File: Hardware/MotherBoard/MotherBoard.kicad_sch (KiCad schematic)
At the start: 16 parts, among them J1 POWER, J10 I/O_PWR, J2 I/O0, J5 I/O1, J6 EXTRN_CLCK, U1 AMS1117-5.0

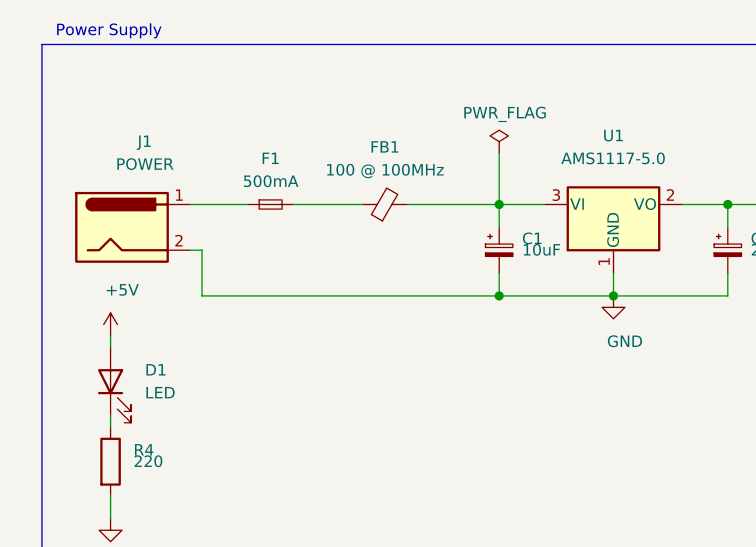
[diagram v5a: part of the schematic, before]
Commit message: Implement DMA and PCB ports
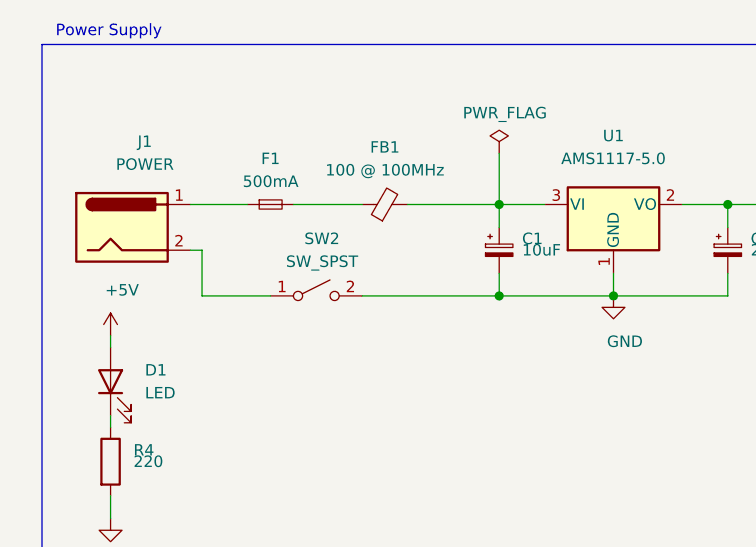
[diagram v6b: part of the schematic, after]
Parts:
- added SW2: SW_SPST, Button_Switch_THT:SW_E-Switch_EG1224_SPDT_Angled, symbol Switch:SW_SPST
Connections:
- net GND: now also SW2.2 (B); no longer J1.2
- new net: J1.2, SW2.1 (A)
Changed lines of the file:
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@@
     (company "Romuald Rousseau")
   )
+  (bus_alias "A12" (members "A12"))
   (bus_alias "A11" (members "A11"))
-  (bus_alias "A12" (members "A12"))
   (junction (at 76.835 47.625) (diameter 1.016) (color 0 0 0 0))
   (junction (at 76.835 57.785) (diameter 1.016) (color 0 0 0 0))
@@
     (stroke (width 0) (type solid) (color 0 0 0 0))
   )
-  (wire (pts (xy 43.815 57.785) (xy 76.835 57.785))
+  (wire (pts (xy 43.815 57.785) (xy 51.435 57.785))
     (stroke (width 0) (type solid) (color 0 0 0 0))
   )
   (wire (pts (xy 53.975 47.625) (xy 61.595 47.625))
+    (stroke (width 0) (type solid) (color 0 0 0 0))
+  )
+  (wire (pts (xy 61.595 57.785) (xy 76.835 57.785))
     (stroke (width 0) (type solid) (color 0 0 0 0))
   )
@@
     )
     (property "Datasheet" "~" (id 3) (at 33.655 67.31 0)
+      (effects (font (size 1.27 1.27)) hide)
+    )
+  )
+  (symbol (lib_id "Switch:SW_SPST") (at 56.515 57.785 0) (unit 1)
+    (in_bom yes) (on_board yes)
+    (property "Reference" "SW2" (id 0) (at 57.15 51.435 0))
+    (property "Value" "SW_SPST" (id 1) (at 57.15 53.975 0))
+    (property "Footprint" "Button_Switch_THT:SW_E-Switch_EG1224_SPDT_Angled" (id 2) (at 56.515 57.785 0)
+      (effects (font (size 1.27 1.27)) hide)
+    )
+    (property "Datasheet" "~" (id 3) (at 56.515 57.785 0)
       (effects (font (size 1.27 1.27)) hide)
     )
@@
       (reference "R4") (unit 1) (value "220") (footprint "Resistor_THT:R_Axial_DIN0207_L6.3mm_D2.5mm_P10.16mm_Horizontal")
     )
+    (path "/ff7dba36-e011-4018-9878-20ec48c66f8c"
+      (reference "SW2") (unit 1) (value "SW_SPST") (footprint "Button_Switch_THT:SW_E-Switch_EG1224_SPDT_Angled")
+    )
     (path "/4bb875c6-ec17-489d-8848-a58782a512d1"
       (reference "U1") (unit 1) (value "AMS1117-5.0") (footprint "Package_TO_SOT_THT:TO-220-3_Horizontal_TabDown")
@@
       (reference "#PWR0120") (unit 1) (value "GND") (footprint "")
     )
+    (path "/61215041-7d34-4941-9afc-8a556d19a10e/fa8f244d-8541-48fd-8737-6f2ca9b67fa3"
+      (reference "#PWR0133") (unit 1) (value "+5V") (footprint "")
+    )
+    (path "/61215041-7d34-4941-9afc-8a556d19a10e/a07bb74b-eddd-4abc-a5b3-41726b4489b6"
+      (reference "#PWR0134") (unit 1) (value "+5V") (footprint "")
+    )
     (path "/61215041-7d34-4941-9afc-8a556d19a10e/f636ab65-9304-4605-a863-9df3dd0ac4b4"
       (reference "C3") (unit 1) (value "10uF") (footprint "Capacitor_THT:C_Radial_D5.0mm_H11.0mm_P2.00mm")
@@
       (reference "J9") (unit 1) (value "Conn_02x02_Odd_Even") (footprint "Connector_PinHeader_2.54mm:PinHeader_2x02_P2.54mm_Vertical")
     )
+    (path "/61215041-7d34-4941-9afc-8a556d19a10e/0b60bde2-4a50-4611-bec5-b23ac5b9a520"
+      (reference "J11") (unit 1) (value "RDY_PULLUP") (footprint "")
+    )
+    (path "/61215041-7d34-4941-9afc-8a556d19a10e/6014f801-bb1a-4e11-b189-6e0f7a468124"
+      (reference "J12") (unit 1) (value "NMI_PULLUP") (footprint "")
+    )
     (path "/61215041-7d34-4941-9afc-8a556d19a10e/296fe1d1-b4f3-406e-be74-c856810e239d"
       (reference "R1") (unit 1) (value "10K") (footprint "Resistor_THT:R_Axial_DIN0207_L6.3mm_D2.5mm_P10.16mm_Horizontal")
@@
       (reference "R3") (unit 1) (value "10K") (footprint "Resistor_THT:R_Axial_DIN0207_L6.3mm_D2.5mm_P10.16mm_Horizontal")
     )
+    (path "/61215041-7d34-4941-9afc-8a556d19a10e/faba855d-d503-4563-a655-ff79b24d55c8"
+      (reference "R5") (unit 1) (value "10K") (footprint "Resistor_THT:R_Axial_DIN0207_L6.3mm_D2.5mm_P10.16mm_Horizontal")
+    )
     (path "/61215041-7d34-4941-9afc-8a556d19a10e/25f68c31-273a-4a47-b1bc-310d19fac600"
-      (reference "SW1") (unit 1) (value "RESET_SW") (footprint "Button_Switch_THT:SW_PUSH_6mm_H5mm")
+      (reference "SW1") (unit 1) (value "RESET_SW") (footprint "Button_Switch_THT:SW_Tactile_SPST_Angled_PTS645Vx83-2LFS")
     )
     (path "/61215041-7d34-4941-9afc-8a556d19a10e/6cd92b81-0135-4e6c-929c-13ce504ee354"
@@
       (reference "J8") (unit 1) (value "ISA11") (footprint "Connector_PinSocket_2.54mm:PinSocket_1x16_P2.54mm_Vertical")
     )
-    (path "/6cbd16f3-a1f6-4857-8623-5a6775377a9a/1e640dc0-9a9b-4e78-97a7-c4c4fba75621"
-      (reference "U9") (unit 1) (value "74HCT541") (footprint "Package_DIP:DIP-20_W7.62mm")
-    )
-    (path "/6cbd16f3-a1f6-4857-8623-5a6775377a9a/87eea902-e28a-40ef-a5ce-0c008a75322f"
-      (reference "U10") (unit 1) (value "74HCT541") (footprint "Package_DIP:DIP-20_W7.62mm")
+    (path "/6cbd16f3-a1f6-4857-8623-5a6775377a9a/3e3baca0-beca-49b0-b567-bf7be578d698"
+      (reference "U9") (unit 1) (value "SN74LVC245AN") (footprint "Package_DIP:DIP-20_W7.62mm")
+    )
+    (path "/6cbd16f3-a1f6-4857-8623-5a6775377a9a/b9a3a795-f7ea-4f67-9322-90ba34134211"
+      (reference "U10") (unit 1) (value "SN74LVC245AN") (footprint "Package_DIP:DIP-20_W7.62mm")
     )
     (path "/6cbd16f3-a1f6-4857-8623-5a6775377a9a/e8617ace-d039-40cf-88f5-54844f714e69"

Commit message: Version 1.2
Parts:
- added J11: RDY_PULLUP, Connector_PinHeader_2.54mm:PinHeader_1x02_P2.54mm_Vertical, symbol Connector:Conn_01x02_Male
- added J12: NMI_PULLUP, Connector_PinHeader_2.54mm:PinHeader_1x02_P2.54mm_Vertical, symbol Connector:Conn_01x02_Male
- added J13: USB_OTG, Connector_USB:USB_B_OST_USB-B1HSxx_Horizontal, symbol Connector:USB_B
- added J14: IRQ0_PULLUP, Connector_PinHeader_2.54mm:PinHeader_1x02_P2.54mm_Vertical, symbol Connector:Conn_01x02_Male
- added R1, R6: 10K, Resistor_THT:R_Axial_DIN0207_L6.3mm_D2.5mm_P10.16mm_Horizontal, symbol Device:R
- J6: symbol Connector:Conn_01x04_Male -> Connector:Conn_01x04_Female
- SW2: value SW_SPST -> ON_OFF
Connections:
- net +5V: now also J6.4 (Pin_4), J11.2 (Pin_2), J13.1 (VBUS), R1.2, R6.2; no longer J6.1 (Pin_1)
- net ECLOCK: now also J6.2 (Pin_2); no longer J6.3 (Pin_3)
- net GND: now also J1.2, J6.3 (Pin_3), J13.4 (GND); no longer J6.2 (Pin_2), SW2.2 (B)
- net RESET: now also J6.1 (Pin_1); no longer J6.4 (Pin_4)
- net at J1.1: now also SW2.1 (A); no longer F1.1
- new net: J12.2 (Pin_2), R1.1
- new net: J14.2 (Pin_2), R6.1
- new net: F1.1, SW2.2 (B)
- new net IRQ0B: J14.1 (Pin_1)
- new net NMIB: J12.1 (Pin_1)
- new net RDYB: J11.1 (Pin_1)
- no-connect marks 0 -> 3
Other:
- sheet Bus Control ports: added D[0..7], IRQ0B, IRQ1B, IRQB, RDYB; removed none
- sheet Main  ports: added IRQ1B, IRQB; removed none
- sheet Ports ports: added IRQ0B; removed none
- note added: "Connectors and Jumpers"
- note removed: "Connectors I/O"
- moved on the sheet: C1, C2, D1, F1, FB1, H1, H2, H3, H4, J1, J10, J2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

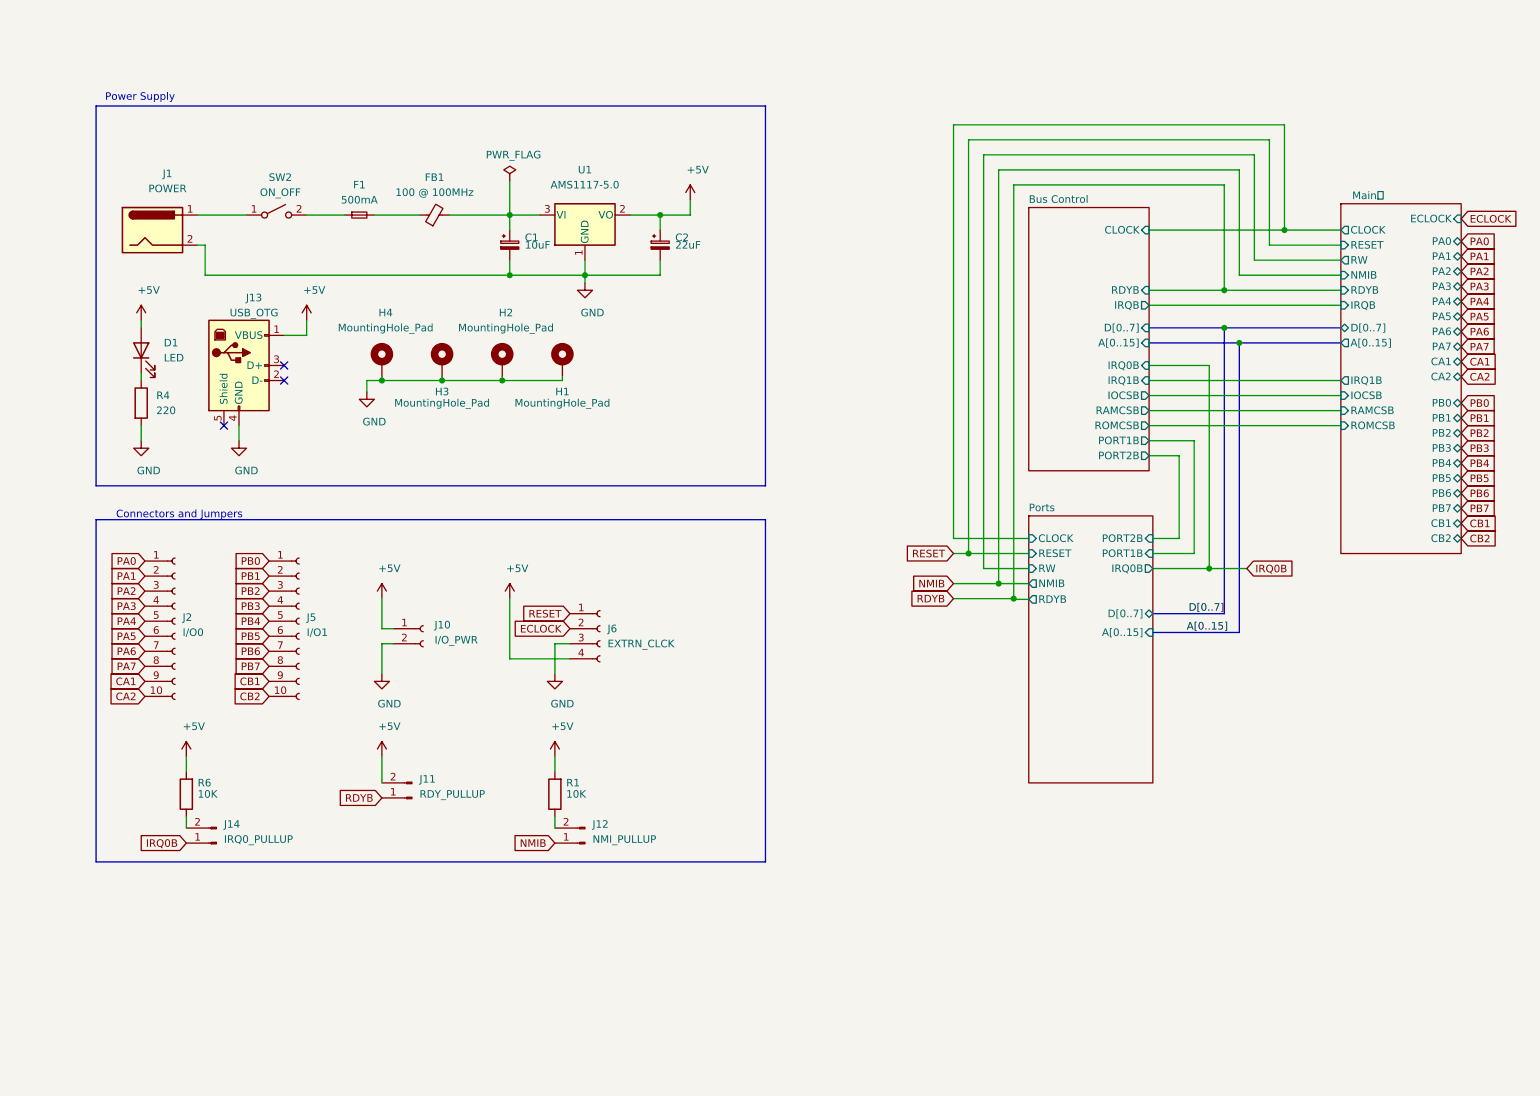
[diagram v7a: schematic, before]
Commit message: New PLD logic, VGA, DMA ...
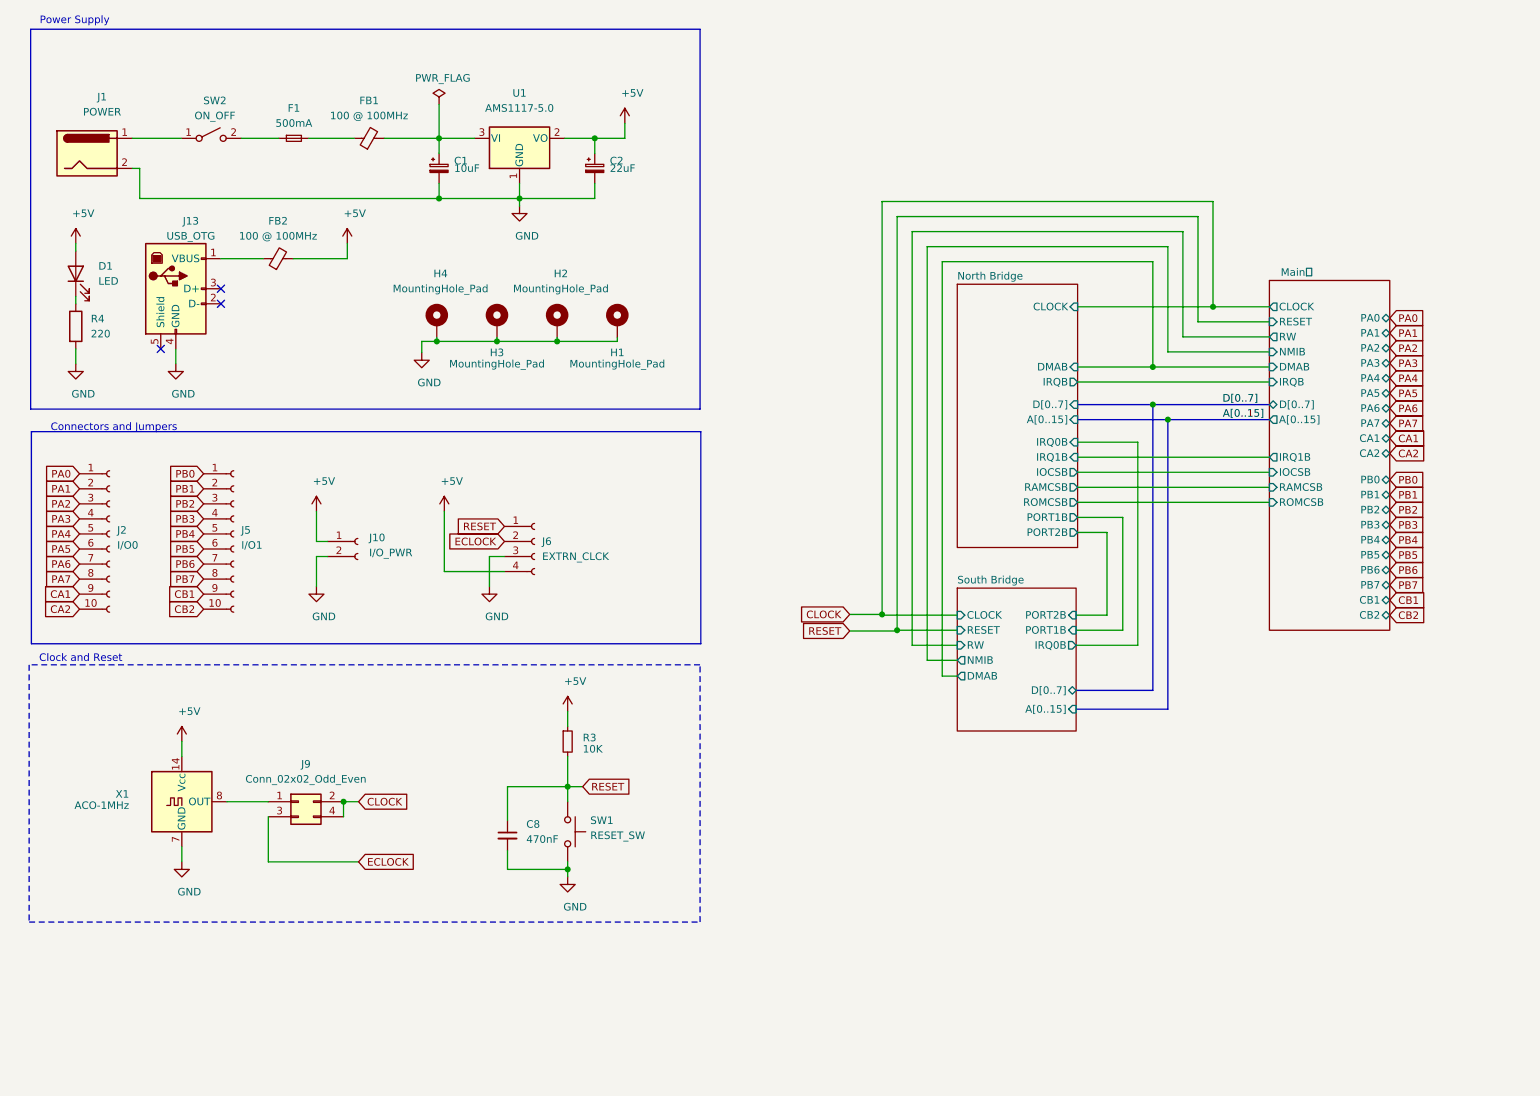
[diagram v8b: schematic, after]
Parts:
- removed J11: RDY_PULLUP, Connector_PinHeader_2.54mm:PinHeader_1x02_P2.54mm_Vertical, symbol Connector:Conn_01x02_Male
- removed J12: NMI_PULLUP, Connector_PinHeader_2.54mm:PinHeader_1x02_P2.54mm_Vertical, symbol Connector:Conn_01x02_Male
- removed J14: IRQ0_PULLUP, Connector_PinHeader_2.54mm:PinHeader_1x02_P2.54mm_Vertical, symbol Connector:Conn_01x02_Male
- removed R1, R6: 10K, Resistor_THT:R_Axial_DIN0207_L6.3mm_D2.5mm_P10.16mm_Horizontal, symbol Device:R
- added C8: 470nF, Capacitor_THT:C_Disc_D5.0mm_W2.5mm_P5.00mm, symbol Device:C_Small
- added FB2: 100 @ 100MHz, Inductor_THT:L_Axial_L9.5mm_D4.0mm_P12.70mm_Horizontal_Fastron_SMCC, symbol Device:Ferrite_Bead_Small
- added J9: Conn_02x02_Odd_Even, Connector_PinHeader_2.54mm:PinHeader_2x02_P2.54mm_Vertical, symbol Connector_Generic:Conn_02x02_Odd_Even
- added R3: 10K, Resistor_THT:R_Axial_DIN0207_L6.3mm_D2.5mm_P10.16mm_Horizontal, symbol Device:R_Small
- added SW1: RESET_SW, Button_Switch_THT:SW_Tactile_SPST_Angled_PTS645Vx83-2LFS, symbol Switch:SW_Push
- added X1: ACO-1MHz, Oscillator:Oscillator_DIP-14, symbol Oscillator:ACO-xxxMHz
- U1: footprint Package_TO_SOT_THT:TO-220-3_Horizontal_TabDown -> Package_TO_SOT_SMD:SOT-223-3_TabPin2
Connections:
- net +5V: now also FB2.2, R3.1, X1.14 (Vcc); no longer J13.1 (VBUS)
- net ECLOCK: now also J9.3 (Pin_3)
- net GND: now also C8.2, SW1.2, X1.7 (GND)
- net RESET: now also C8.1, R3.2, SW1.1
- new net: J9.1 (Pin_1), X1.8 (OUT)
- new net: FB2.1, J13.1 (VBUS)
- new net CLOCK: J9.2 (Pin_2), J9.4 (Pin_4)
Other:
- sheet Bus Control renamed North Bridge
- sheet Ports renamed South Bridge
- sheet Main  ports: added DMAB; removed ECLOCK, RDYB
- sheet North Bridge: file /home/romuald/Projects/Miniish/Hardware/MotherBoard/BusControl.kicad_sch -> /home/romuald/Projects/Miniish/Hardware/MotherBoard/NorthBridge.kicad_sch
- sheet North Bridge ports: added DMAB; removed RDYB
- sheet South Bridge: file BusExtentions.kicad_sch -> /home/romuald/Projects/Miniish/Hardware/MotherBoard/SouthBridge.kicad_sch
- sheet South Bridge ports: added DMAB; removed RDYB
- note added: "Clock and Reset"
- moved on the sheet: C1, C2, D1, F1, FB1, H1, H2, H3, H4, J1, J10, J13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
